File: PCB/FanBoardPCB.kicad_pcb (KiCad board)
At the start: 2 copper layers, 40 x 37.9 mm, 29 parts, among them J1 Conn_01x02_Pin, J2 Conn_01x02_Pin, J3 Conn_01x02_Pin, J4 Conn_01x02_Pin, J5 FanBrdConn, Q1 IRLML0030, Q2 IRLML0030, Q3 IRLML0030, Q4 IRLML0030

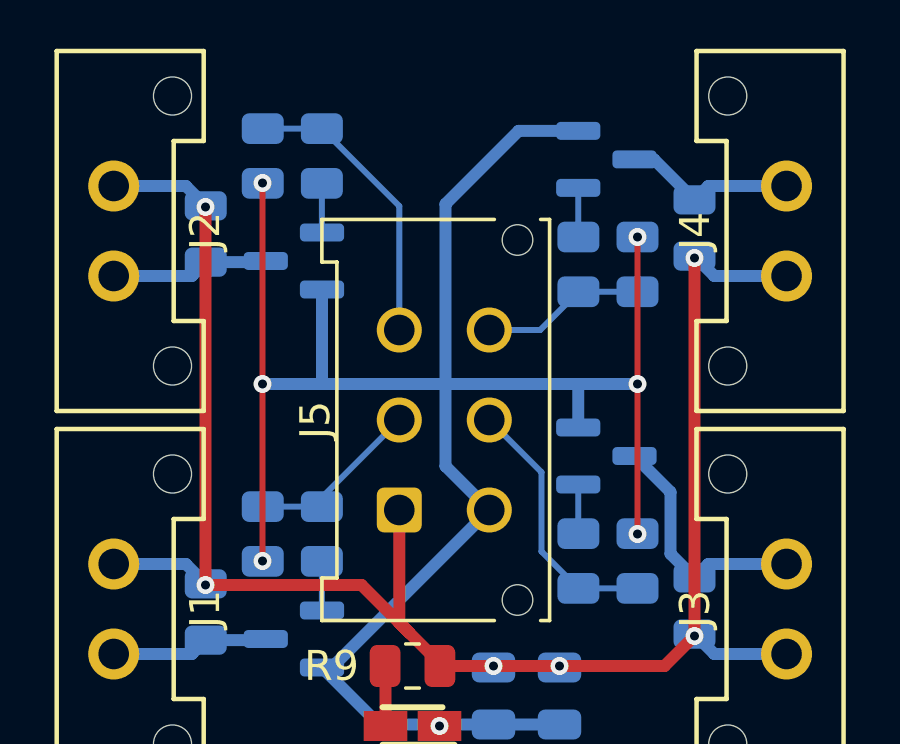
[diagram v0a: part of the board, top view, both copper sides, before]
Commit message: moved some traces
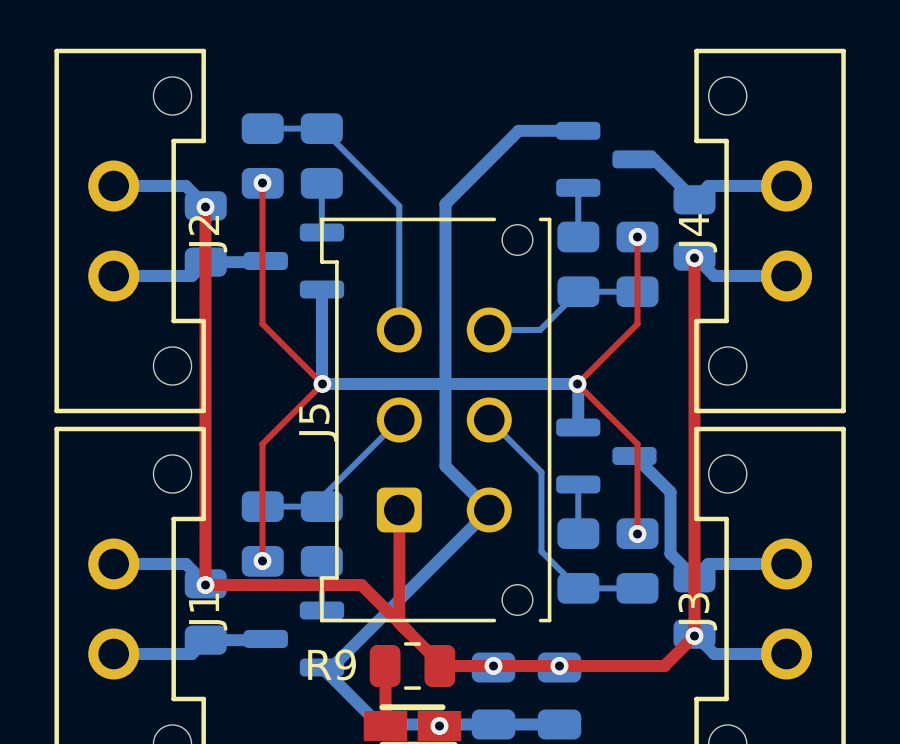
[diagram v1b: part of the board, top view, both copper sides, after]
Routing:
- net GNDPWR: track 72.9 -> 71.7 mm
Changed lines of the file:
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@@
+	)
+	(segment
+		(start 94.1 115.4)
+		(end 92.1 113.4)
+		(width 0.2)
+		(layer "F.Cu")
+		(net 1)
 	)
 	(segment
 		(start 94.1 108.5)
-		(end 94.1 118.4)
-		(width 0.2)
-		(layer "F.Cu")
-		(net 1)
-	)
-	(segment
-		(start 81.6 113.4)
-		(end 81.6 106.7)
-		(width 0.2)
-		(layer "F.Cu")
-		(net 1)
-	)
-	(segment
-		(start 81.6 119.3)
-		(end 81.6 113.4)
-		(width 0.2)
-		(layer "F.Cu")
-		(net 1)
-	)
-	(via
-		(at 94.1 113.4)
-		(size 0.6)
-		(drill 0.3)
-		(layers "F.Cu" "B.Cu")
-		(free yes)
+		(end 94.1 111.4)
+		(width 0.2)
+		(layer "F.Cu")
+		(net 1)
+	)
+	(segment
+		(start 81.6 111.4)
+		(end 83.6 113.4)
+		(width 0.2)
+		(layer "F.Cu")
+		(net 1)
+	)
+	(segment
+		(start 81.6 115.4)
+		(end 81.6 119.3)
+		(width 0.2)
+		(layer "F.Cu")
+		(net 1)
+	)
+	(segment
+		(start 81.6 106.7)
+		(end 81.6 111.4)
+		(width 0.2)
+		(layer "F.Cu")
+		(net 1)
+	)
+	(segment
+		(start 83.6 113.4)
+		(end 81.6 115.4)
+		(width 0.2)
+		(layer "F.Cu")
+		(net 1)
+	)
+	(segment
+		(start 94.1 118.4)
+		(end 94.1 115.4)
+		(width 0.2)
+		(layer "F.Cu")
+		(net 1)
+	)
+	(segment
+		(start 94.1 111.4)
+		(end 92.1 113.4)
+		(width 0.2)
+		(layer "F.Cu")
+		(net 1)
+	)
+	(via
+		(at 92.1 113.4)
+		(size 0.6)
+		(drill 0.3)
+		(layers "F.Cu" "B.Cu")
 		(net 1)
 	)
@@
 	)
 	(via
+		(at 83.6 113.4)
+		(size 0.6)
+		(drill 0.3)
+		(layers "F.Cu" "B.Cu")
+		(net 1)
+	)
+	(via
 		(at 94.1 118.4)
 		(size 0.6)
@@
 	(via
 		(at 81.6 106.7)
-		(size 0.6)
-		(drill 0.3)
-		(layers "F.Cu" "B.Cu")
-		(net 1)
-	)
-	(via
-		(at 81.6 113.4)
 		(size 0.6)
 		(drill 0.3)
@@
 	)
 	(segment
-		(start 94.1 113.4)
-		(end 92.6 113.4)
-		(width 0.4)
-		(layer "B.Cu")
-		(net 1)
-	)
-	(segment
-		(start 92.6 113.4)
-		(end 92.1 113.4)
-		(width 0.4)
-		(layer "B.Cu")
-		(net 1)
-	)
-	(segment
 		(start 87.7 107.4)
 		(end 90.137499 104.962501)
@@
 	)
 	(segment
-		(start 92.125 113.425)
-		(end 92.1 113.4)
-		(width 0.4)
-		(layer "B.Cu")
-		(net 1)
-	)
-	(segment
 		(start 90.137499 104.962501)
 		(end 92.125 104.962501)
@@
 	)
 	(segment
-		(start 92.125 114.850001)
-		(end 92.125 113.425)
-		(width 0.4)
-		(layer "B.Cu")
-		(net 1)
-	)
-	(segment
 		(start 89.16 117.6)
 		(end 87.7 116.14)
@@
 	)
 	(segment
+		(start 92.1 113.4)
+		(end 92.125 113.425)
+		(width 0.4)
+		(layer "B.Cu")
+		(net 1)
+	)
+	(segment
 		(start 89.16 117.6)
 		(end 83.91 122.85)
@@
 	)
 	(segment
-		(start 92.6 113.4)
-		(end 83.6 113.4)
+		(start 83.6 113.4)
+		(end 92.1 113.4)
 		(width 0.4)
 		(layer "B.Cu")
@@
 	)
 	(segment
-		(start 83.6 113.4)
-		(end 81.6 113.4)
-		(width 0.4)
-		(layer "B.Cu")
+		(start 92.125 113.425)
+		(end 92.125 114.850001)
+		(width 0.4)
+		(layer "B.Cu")

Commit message: fixed
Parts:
- R9: moved to B.Cu
- moved H3 5.40 mm to (76.4, 130.6)
- moved H1 5.30 mm to (76.2, 98.7)
- moved H4 4.81 mm to (99.2, 130.5)
- moved H2 4.75 mm to (99.3, 98.7)
- moved LED1 2.05 mm to (87.1, 122.8), turned to 0 degrees
- moved C1 0.92 mm to (92.4, 124.0)
- moved C2 0.92 mm to (90.2, 124.0)
- moved Q2 0.88 mm to (82.7, 108.4)
- moved R3 0.88 mm to (81.7, 104.9)
- moved R4 0.88 mm to (83.7, 104.9)
- moved Q1 0.67 mm to (82.7, 121.2)
- moved R2 0.67 mm to (83.7, 117.7)
- moved R1 0.67 mm to (81.7, 117.7)
- moved R9 0.46 mm to (87.1, 122.8), turned to 0 degrees
- moved Q3 0.11 mm to (93.0, 115.8)
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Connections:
- LED1 pad 1: GNDPWR -> Net-(LED1-K)
- LED1 pad 2: Net-(LED1-A) -> +12V
- R9 pad 1: +12V -> Net-(LED1-K)
- R9 pad 2: Net-(LED1-A) -> GNDPWR
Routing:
- net GNDPWR: track 71.7 -> 9.94 mm, vias 7 -> 3
- net +12V: track 60.8 -> 13.4 mm
- net Net-(LED1-A): track 2.01 -> 0.00 mm
- net FAN2: track 9.75 -> 10.6 mm
- net FAN1: track 5.93 -> 5.37 mm
- net Net-(LED1-K): vias 0 -> 1
- added copper zone on F.Cu, net +12V
- added copper zone on B.Cu, net GNDPWR
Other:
- board size 40 x 37.9 mm -> 30.3 x 39.3 mm

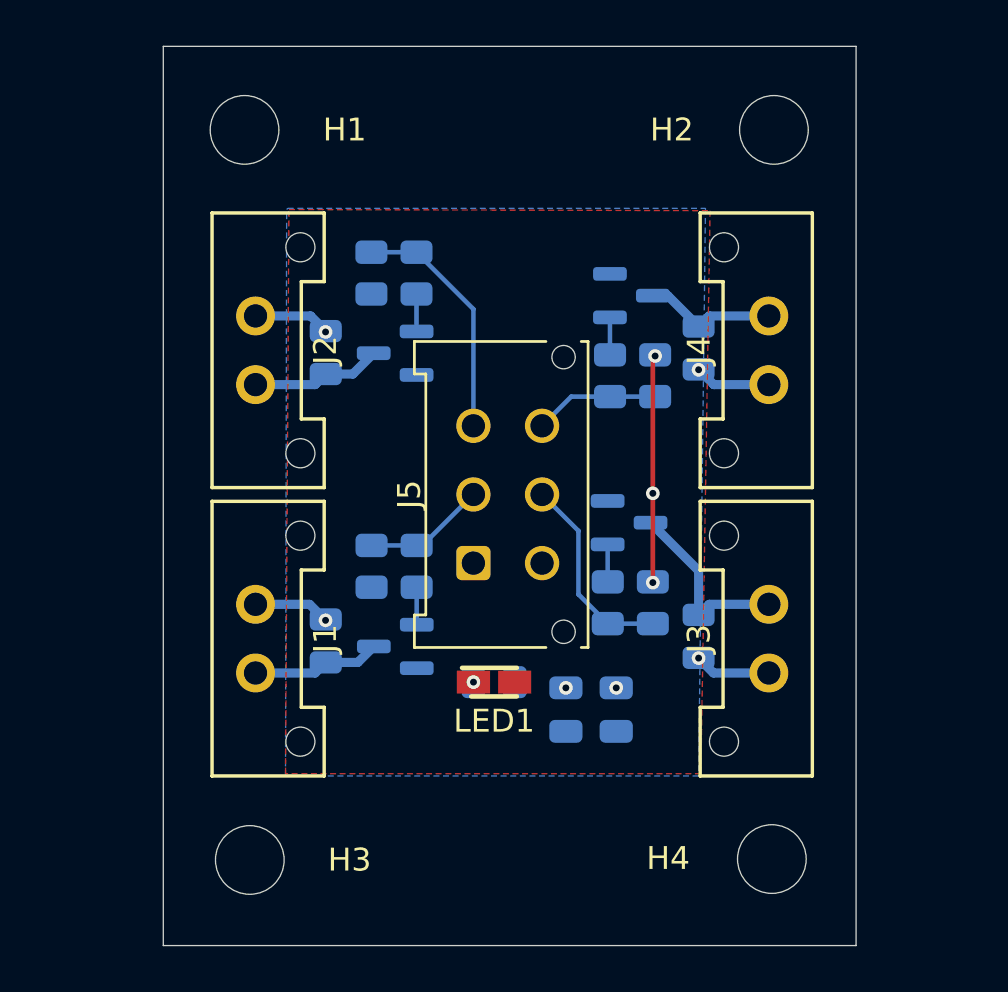
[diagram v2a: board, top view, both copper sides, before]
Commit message: fan labels
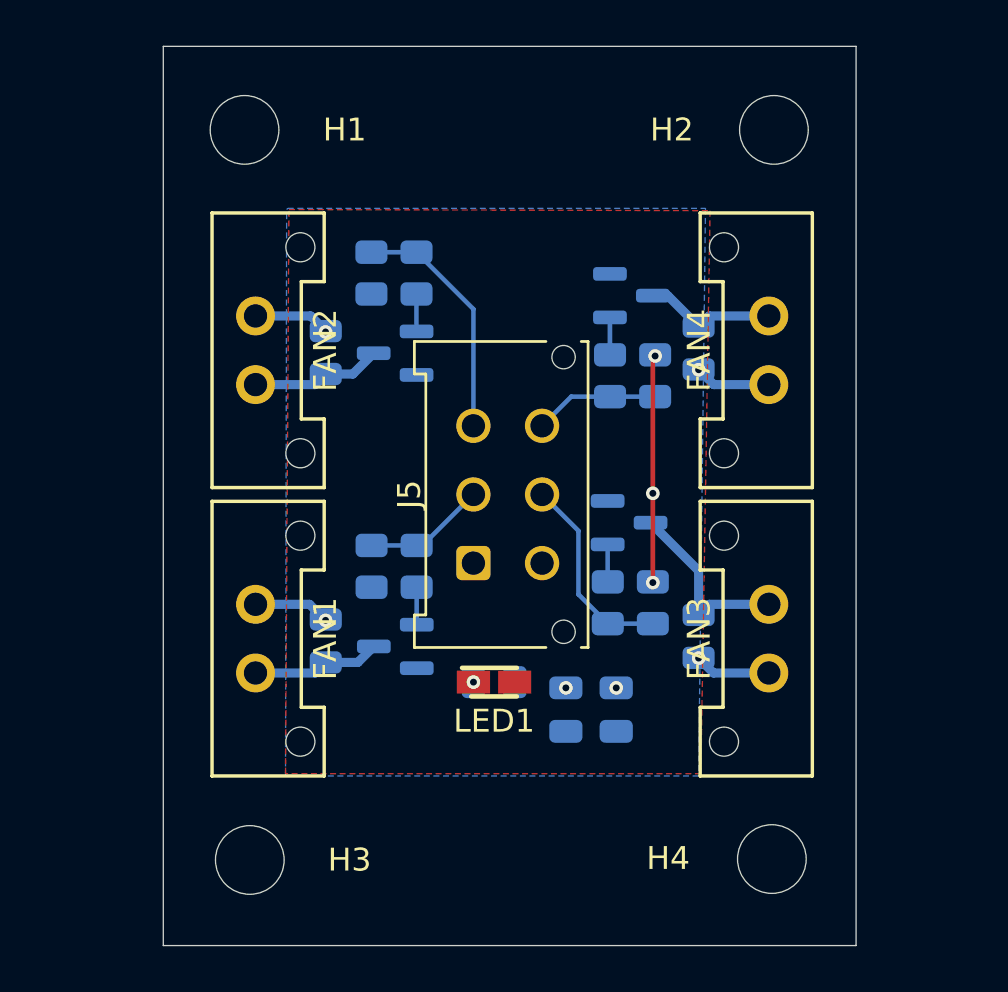
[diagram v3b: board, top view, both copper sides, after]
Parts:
- renumbered J1 to FAN1, J2 to FAN2, J3 to FAN3, J4 to FAN4
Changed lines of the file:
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@@
 		(layer "F.Cu")
 		(at 76.64 119.4 -90)
-		(property "Reference" "J1"
-			(at 1.5 -3.05 -90)
+		(property "Reference" "FAN1"
+			(at 1.5 -3.05 270)
 			(layer "F.SilkS")
 			(effects
@@
 		(layer "F.Cu")
 		(at 99.06875 122.4 90)
-		(property "Reference" "J3"
+		(property "Reference" "FAN3"
 			(at 1.5 -3.05 90)
 			(layer "F.SilkS")
@@
 		(layer "F.Cu")
 		(at 99.06875 109.8 90)
-		(property "Reference" "J4"
+		(property "Reference" "FAN4"
 			(at 1.5 -3.05 90)
 			(layer "F.SilkS")
@@
 		(layer "F.Cu")
 		(at 76.64 106.8 -90)
-		(property "Reference" "J2"
+		(property "Reference" "FAN2"
 			(at 1.5 -3.05 90)
 			(layer "F.SilkS")

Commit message: testpoints
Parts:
- added 12V: 12VTP, TestPoint:TestPoint_Pad_1.0x1.0mm, F.Cu at (89.4, 103.7)
- added GND: GNDTP, TestPoint:TestPoint_Pad_1.0x1.0mm, F.Cu at (85.9, 103.7)
- renumbered FAN1 to J1, FAN2 to J2, FAN3 to J3, FAN4 to J4
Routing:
- net GNDPWR: vias 3 -> 4
